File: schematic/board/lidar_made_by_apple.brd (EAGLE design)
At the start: 79.9 x 73.5 mm, 85 parts, among them J1 U.FL-R-SMT-1_10_, J2 U.FL-R-SMT-1_10_

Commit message: спонсор страданий
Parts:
- removed JP1, JP2: (no value), NEON-BLADE-2024:1X08
- removed W2: (no value), NEON-BLADE-2024:SOLDERING-PAD-4A
- added JP3: (no value), pinhead:1X15
- added JP4, JP5: (no value), pinhead:1X09
- added U$12, U$14: REF3033, NEON-BLADE-2024:SOT23-3
- added VR1, VR2: 3362P-1-502LF, NEON-BLADE-2024:TRIM_3362P-1-502LF
- added W5: (no value), NEON-BLADE-2024:SOLDERING-PAD-4A
- moved W1 38.3 mm to (22.7, 59.8)
- moved L9 18.0 mm to (38.1, 71.5)
- moved R30 13.8 mm to (37.9, 74.2), turned to 180 degrees
- moved C18 6.21 mm to (40.9, 77.2), turned to 180 degrees
- moved R21 5.83 mm to (48.3, 75.1)
- moved C9 5.10 mm to (68.2, 29.8)
- moved D2 4.58 mm to (65.8, 30.2), turned to 180 degrees
- moved C20 4.00 mm to (43.1, 73.0)
- moved C21 3.00 mm to (57.3, 69.4)
- moved C22 3.00 mm to (57.3, 72.7)
- moved C29 3.00 mm to (60.0, 69.9)
- moved R24 3.00 mm to (54.6, 70.6)
- moved R31 3.00 mm to (58.0, 66.7)
- moved U$10 3.00 mm to (48.0, 68.9)
- moved U$9 3.00 mm to (52.0, 70.5)
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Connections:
- removed net MISO: JP2.5, U$10.12
- removed net MOSI: JP2.6, U$10.11
- removed net SCK: JP2.4, U$10.10
- removed net SSN: JP2.3, U$10.9
- removed net VIN: L2.2, L4.1
- new net 1MISO: JP3.3
- new net 1MOSI: JP3.2
- new net 1SCK: JP3.1
- new net 4MISO: JP5.4, U$10.12
- new net 4MOSI: JP5.3, U$10.11
- new net 4SCK: JP5.2, U$10.10
- new net 5MISO: JP3.11
- new net 5MOSI: JP3.10
- new net 5SCK: JP3.9
- new net 5V: JP4.1
- new net CE_NRF: JP3.7
- new net CS_LIS: JP3.4
- new net CS_LSM: JP3.12
- new net CS_NRF: JP3.8
- new net CS_TDC: JP5.5, U$10.9
- new net N$28: JP3.13
- new net N$30: JP3.15
- new net N$33: R6.1, VR1.1
- new net N$35: R5.2, VR1.3
- new net N$37: R22.1, VR2.1
- new net N$38: R23.2, VR2.3
- new net SCL: JP4.9
- new net SDA: JP4.8
- new net SDIO_CK: JP4.5
- new net SDIO_CMD: JP4.4
- new net SDIO_DAT0: JP4.6
- new net SDIO_DAT1: JP4.7
- new net SDIO_DAT2: JP4.2
- new net SDIO_DAT3: JP4.3
- new net USIL_ON: JP5.1
- new net V_BAT: JP3.14, L2.2, L4.1, U$12.1, U$14.1
- net 3V3: now also JP3.5, U$12.2, U$14.2; no longer JP2.8
- net AGND: now also R26.1, U$12.3, U$14.3, W5.P$2
- net APD_FB_VOLT: now also JP5.8; no longer JP1.7
- net APD_PWM: now also JP5.9; no longer JP1.8
- net GND: now also JP3.6, W5.P$1; no longer JP2.7, R26.1, W2.P$2
- net LASER_COMP: now also JP5.6; no longer JP1.2
- net LGND: no longer W2.P$1
- net N$27: now also VR1.2; no longer R5.2, R6.1
- net N$5: now also VR2.2; no longer R22.1, R23.2
- net TDC_INT: now also JP5.7; no longer JP1.3

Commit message: переделал плату лидара
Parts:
- removed R4: 10k, rcl:R0603
- removed U$14: REF3033, NEON-BLADE-2024:SOT23-3
- moved C24 146.4 mm to (-69.8, 41.9), turned to 0 degrees
- moved C21 127.9 mm to (-68.6, 47.0), turned to 0 degrees
- moved C17 127.2 mm to (-62.2, 47.0)
- moved R1 99.4 mm to (-61.0, 62.2), turned to 0 degrees
- moved C22 77.9 mm to (-17.8, 52.1), turned to 0 degrees
- moved C33 72.4 mm to (-33.0, 35.6)
- moved R30 58.7 mm to (47.0, 16.2), turned to 90 degrees
- moved R21 57.1 mm to (43.5, 18.2), turned to 270 degrees
- moved L9 56.5 mm to (44.4, 15.3)
- moved C18 51.7 mm to (42.1, 25.5), turned to 0 degrees
- moved C20 51.4 mm to (42.1, 21.6)
- moved L2 49.2 mm to (65.2, 76.3), turned to 90 degrees
- moved C29 47.9 mm to (59.5, 22.0), turned to 0 degrees
- moved R31 46.8 mm to (59.5, 19.9), turned to 0 degrees
- moved R24 45.2 mm to (58.0, 25.5)
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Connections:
- removed net LASER_DAC: R4.2
- removed net LGND: C16.2, C17.1, C2.1, C9.1, J2.2, R16.1, R19.1, R6.2, U$1.P$4, U$1.P$5, U$11.GND, W1.P$1, W3.1
- removed net N$19: U$2.P$1, U$2.P$2
- new net 3V3_REF: C24.1, L10.1, L7.1, U$12.2, U$4.P$5
- new net PGND: C16.2, C17.1, C2.1, C6.2, C9.1, J2.2, R16.1, R19.1, R6.2, U$1.P$4, U$1.P$5, U$11.GND, W1.P$1, W3.1
- net 3V3: no longer C24.1, L10.1, L7.1, U$12.2, U$14.2, U$4.P$5
- net AGND: no longer U$14.3
- net GND: no longer C6.2
- net N$27: no longer R4.1
- net N$4: now also U$2.P$1, U$2.P$2
- net V_BAT: no longer U$14.1

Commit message: я сделял
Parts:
- moved C17 137.4 mm to (75.0, 54.5)
- moved C21 129.7 mm to (59.7, 28.0), turned to 180 degrees
- moved C24 118.3 mm to (48.4, 38.5), turned to 180 degrees
- moved R1 101.2 mm to (37.1, 37.0)
- moved C22 80.3 mm to (59.7, 31.0), turned to 180 degrees
- moved C33 67.0 mm to (34.0, 37.0), turned to 180 degrees
- moved R31 10.7 mm to (64.5, 29.3), turned to 90 degrees
- moved C29 7.87 mm to (62.4, 29.3), turned to 90 degrees
- moved U$2 7.12 mm to (75.7, 51.5), turned to 0 degrees
- moved R18 6.37 mm to (78.4, 54.5), turned to 0 degrees
- moved C19 6.21 mm to (57.5, 53.2), turned to 0 degrees
- moved R24 4.12 mm to (57.0, 29.5)
- moved U$9 4.12 mm to (54.5, 29.5)
- moved C16 2.83 mm to (78.2, 62.0), turned to 90 degrees
- moved C9 2.01 mm to (74.2, 71.0)
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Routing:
- net GND: track 0.00 -> 173.5 mm, vias 0 -> 8
- net 3V3: track 0.00 -> 130.0 mm, vias 0 -> 3
- net PGND: track 0.00 -> 85.2 mm, vias 0 -> 2
- net AGND: track 0.00 -> 66.7 mm, vias 0 -> 2
- net LASER_COMP: track 0.00 -> 62.5 mm, vias 0 -> 1
- net LASER_PULSE: track 0.00 -> 62.4 mm, vias 0 -> 3
- net V_BAT: track 0.00 -> 54.2 mm, vias 0 -> 2
- net APD_FB_VOLT: track 0.00 -> 53.8 mm, vias 0 -> 1
- net APD_PWM: track 0.00 -> 50.1 mm, vias 0 -> 1
- net TDC_INT: track 0.00 -> 46.3 mm
- net CS_TDC: track 0.00 -> 39.3 mm
- net I_LASER: track 0.00 -> 39.0 mm
- net APD_COMP_OUT: track 0.00 -> 37.4 mm
- net APD_V: track 0.00 -> 35.4 mm, vias 0 -> 2
- net VLASER: track 0.00 -> 34.5 mm
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
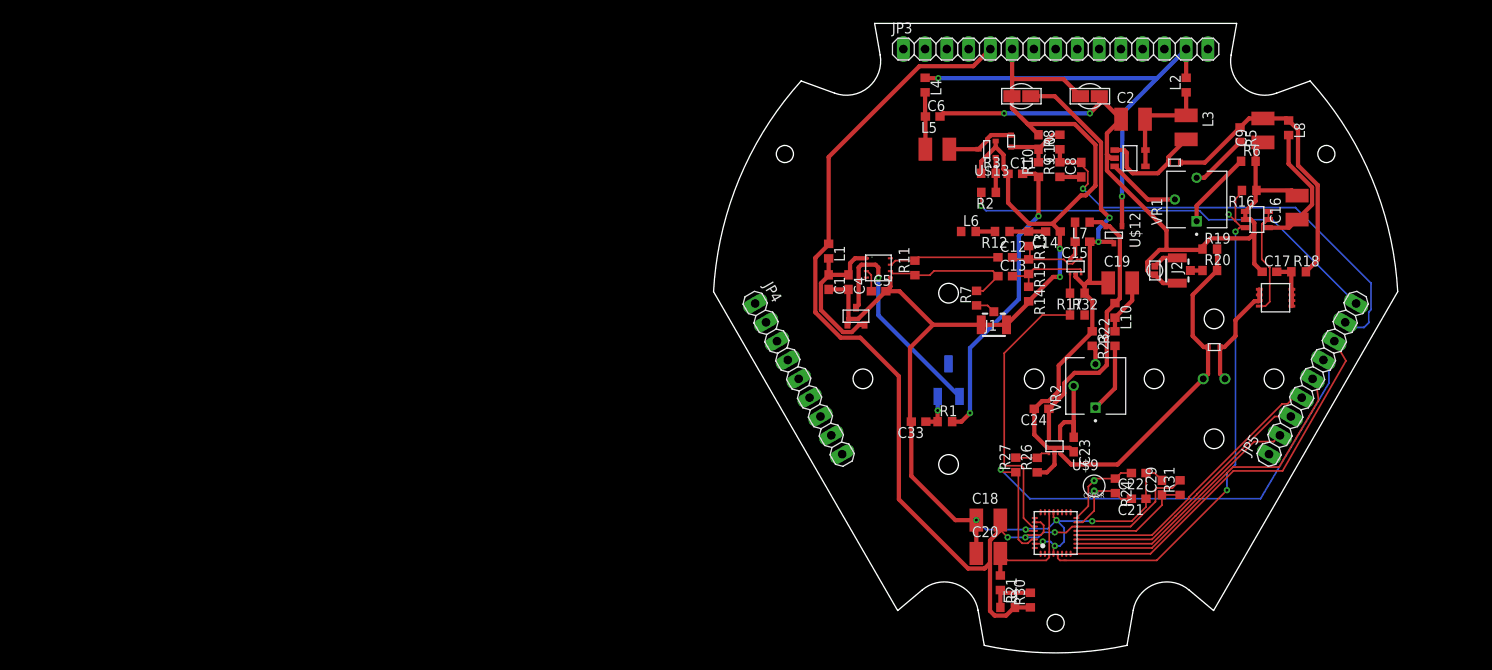
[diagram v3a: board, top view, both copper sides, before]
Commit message: немного переделал плату лидара
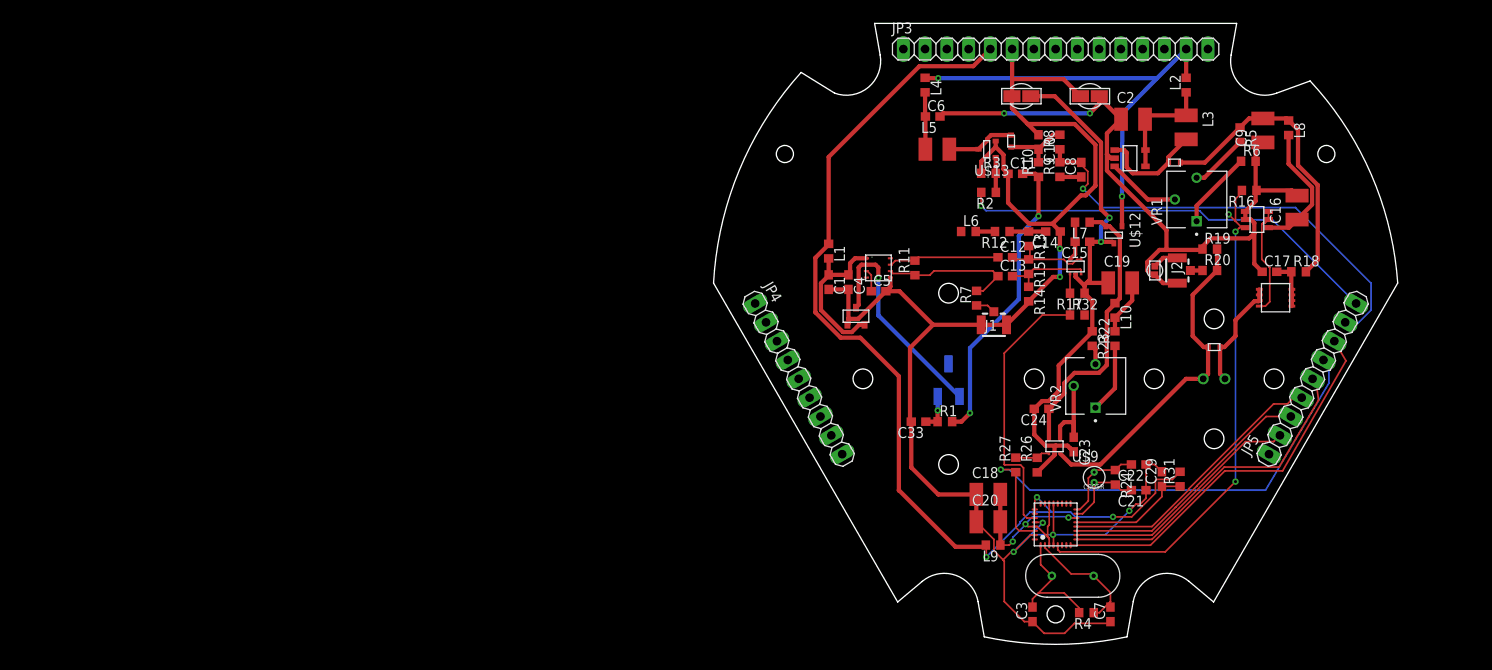
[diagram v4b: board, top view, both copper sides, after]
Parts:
- removed R21: 22, rcl:R0603
- removed R30: 0, rcl:R0603
- added C3, C7: 15pF, rcl:C0603
- added R4: 560k, rcl:R0603
- added U$14: HC49S, NEON-BLADE-2024:HC49S
- moved L9 7.48 mm to (42.7, 22.6), turned to 180 degrees
- moved C20 3.70 mm to (42.1, 25.3)
- moved C18 3.00 mm to (42.1, 28.5)
- moved C21 1.00 mm to (59.7, 29.0)
- moved C22 1.00 mm to (59.7, 32.0)
- moved C29 1.00 mm to (62.4, 30.3)
- moved R24 1.00 mm to (57.0, 30.5)
- moved R31 1.00 mm to (64.5, 30.3)
- moved U$10 1.00 mm to (50.0, 25.0)
- moved U$9 1.00 mm to (54.5, 30.5)
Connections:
- removed net N$24: L9.1, R21.2, R30.2
- removed net TDC_CLK: U$10.1
- new net N$19: C7.2, R4.1, U$10.2, U$14.P$1
- new net V_TDC: C18.2, C20.2, L9.1, U$10.14, U$10.22, U$10.29, U$10.3
- net 3V3: no longer C18.2, R30.1, U$10.14, U$10.29
- net GND: now also C3.1, C7.1
- net N$23: now also C3.2, R4.2, U$10.1, U$14.P$2; no longer C20.2, R21.1, U$10.22, U$10.3
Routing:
- net V_TDC: track 0.00 -> 25.5 mm, vias 0 -> 3
- net GND: track 173.5 -> 198.3 mm, vias 8 -> 6
- net N$19: track 0.00 -> 14.3 mm
- net 3V3: track 130.0 -> 116.1 mm
- net N$24: track 5.66 -> 0.00 mm
- net LASER_COMP: track 62.5 -> 60.1 mm
- net APD_FB_VOLT: track 53.8 -> 53.1 mm
- net N$23: track 14.0 -> 14.7 mm
- net APD_COMP_OUT: track 37.4 -> 36.7 mm
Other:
- board size 79.9 x 73.5 mm -> 79.9 x 72.5 mm

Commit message: ага угу
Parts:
- moved W5 31.9 mm to (63.0, 48.0), turned to 0 degrees
- moved U$5 5.00 mm to (32.3, 59.0)
- moved C1 5.00 mm to (26.5, 57.3)
- moved C4 5.00 mm to (28.8, 57.3)
- moved C5 5.00 mm to (32.3, 56.2)
- moved D6 5.00 mm to (29.7, 53.3)
- moved L1 5.00 mm to (26.5, 60.9)
- moved R11 5.00 mm to (36.6, 59.0)
- moved J2 2.00 mm to (66.2, 54.6)
- moved R19 2.00 mm to (70.0, 57.1)
- moved R20 2.00 mm to (70.0, 54.6)
- moved W3 2.00 mm to (63.6, 54.6)
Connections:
- net AGND: now also C1.2, C14.1, C33.2, C4.2, C5.2, D6.P$1, J1.1, J1.2, R14.2, U$5.P$5
- net GND: no longer C1.2, C10.1, C11.1, C14.1, C33.2, C4.2, C5.2, D6.P$1, J1.1, J1.2, R14.2, R3.1, U$13.2, U$5.P$5
- net PGND: now also C10.1, C11.1, R3.1, U$13.2
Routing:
- net GND: track 198.3 -> 129.4 mm, vias 6 -> 4
- net AGND: track 66.8 -> 128.5 mm
- net APD_V: track 35.4 -> 83.9 mm
- net PGND: track 85.2 -> 116.2 mm
- net APD_FB_VOLT: track 53.1 -> 57.4 mm
- net 3V3: track 116.1 -> 112.3 mm
- net N$8: track 26.4 -> 29.1 mm
- net I_LASER: track 39.0 -> 40.8 mm, vias 0 -> 1
- net N$11: track 16.4 -> 14.7 mm
- net APD_PWM: track 50.1 -> 51.0 mm
- net LASER_PULSE: track 61.9 -> 62.8 mm

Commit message: Безумие — это точное повторение одного и того же действия раз за разом в надежде на изменение
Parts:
- moved L9 55.4 mm to (43.1, 78.0)
- moved U$10 48.3 mm to (49.0, 73.3)
- moved U$14 47.8 mm to (47.5, 66.6)
- moved R4 47.8 mm to (47.5, 62.1)
- moved C18 46.5 mm to (42.5, 75.0)
- moved C20 46.5 mm to (42.5, 71.8)
- moved L4 46.3 mm to (58.0, 36.2)
- moved C7 45.2 mm to (48.6, 59.0)
- moved C6 44.9 mm to (60.6, 35.3)
- moved C3 44.5 mm to (46.4, 59.0)
- moved C21 44.3 mm to (59.1, 73.3)
- moved C22 44.3 mm to (59.1, 76.3)
- moved R24 44.3 mm to (56.4, 74.8)
- moved U$9 44.3 mm to (53.9, 74.8)
- moved D1 44.0 mm to (60.8, 28.8)
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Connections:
- net 3V3: no longer L1.1, R31.2, U$10.25, U$10.26
- net 3V3_REF: now also L1.1
- net V_TDC: now also R31.2, U$10.25, U$10.26
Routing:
- net 3V3: track 112.3 -> 2.56 mm, vias 3 -> 0
- net APD_V: track 83.9 -> 23.2 mm, vias 2 -> 0
- net GND: track 129.4 -> 69.9 mm, vias 4 -> 3
- net PGND: track 116.2 -> 165.6 mm, vias 2 -> 0
- net 3V3_REF: track 33.0 -> 70.1 mm, vias 0 -> 2
- net VLASER: track 34.5 -> 8.81 mm
- net APD_FB_VOLT: track 57.4 -> 33.1 mm, vias 1 -> 0
- net I_LASER: track 40.8 -> 17.8 mm, vias 1 -> 0
- net LASER_PULSE: track 62.8 -> 40.0 mm, vias 3 -> 2
- net N$17: track 4.22 -> 24.7 mm
- net 4SCK: track 28.6 -> 48.9 mm, vias 0 -> 1
- net 4MISO: track 32.6 -> 52.1 mm, vias 0 -> 1
- net 4MOSI: track 30.6 -> 50.0 mm, vias 0 -> 1
- net N$8: track 29.1 -> 11.7 mm
- net N$13: track 4.32 -> 19.8 mm
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- added copper zone on layer 16, net AGND
- added copper zone on layer 16, net GND
- added copper zone on layer 16, net PGND
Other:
- outline, holes or cut-outs redrawn

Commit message: Даниил на протяжении 510 лет переделывает плату лидара
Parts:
- moved C3 2.70 mm to (44.9, 61.2)
- moved C7 2.70 mm to (50.1, 61.2)
- moved C16 1.00 mm to (78.4, 62.1)
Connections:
- net 5V: now also U$12.1
- net V_BAT: no longer U$12.1
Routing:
- net 5V: track 0.00 -> 43.6 mm, vias 0 -> 1
- net V_BAT: track 65.0 -> 73.6 mm, vias 3 -> 2
- net LASER_COMP: track 73.8 -> 72.0 mm, vias 3 -> 4
- net APD_COMP_OUT: track 37.6 -> 39.2 mm
- net PGND: track 165.6 -> 164.2 mm
- net N$23: track 12.7 -> 12.1 mm
- net N$19: track 12.7 -> 12.1 mm

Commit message: почти добавил новый разъём
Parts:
- removed JP3: (no value), pinhead:1X15
- removed JP4, JP5: (no value), pinhead:1X09
- added U$15, U$16: PBS_SMD_X9, NEON-BLADE-2024:PBS_SMD_X9
- added U$17: PBS_SMD_X15, NEON-BLADE-2024:PBD_SMD_X15
- moved C21 3.24 mm to (62.3, 73.8)
- moved C22 3.22 mm to (62.3, 75.9)
- moved L9 1.17 mm to (42.5, 77.0)
- moved C18 1.00 mm to (42.5, 74.0)
- moved C20 1.00 mm to (42.5, 70.8)
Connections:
- net 1MISO: now also U$17.3; no longer JP3.3
- net 1MOSI: now also U$17.2; no longer JP3.2
- net 1SCK: now also U$17.1; no longer JP3.1
- net 3V3: now also U$17.5; no longer JP3.5
- net 4MISO: now also U$15.4; no longer JP5.4
- net 4MOSI: now also U$15.3; no longer JP5.3
- net 4SCK: now also U$15.2; no longer JP5.2
- net 5MISO: now also U$17.11; no longer JP3.11
- net 5MOSI: now also U$17.10; no longer JP3.10
- net 5SCK: now also U$17.9; no longer JP3.9
- net 5V: now also U$16.1; no longer JP4.1
- net APD_FB_VOLT: now also U$15.8; no longer JP5.8
- net APD_PWM: now also U$15.9; no longer JP5.9
- net CE_NRF: now also U$17.7; no longer JP3.7
- net CS_LIS: now also U$17.4; no longer JP3.4
- net CS_LSM: now also U$17.12; no longer JP3.12
- net CS_NRF: now also U$17.8; no longer JP3.8
- net CS_TDC: now also U$15.5; no longer JP5.5
- net GND: now also U$17.6; no longer JP3.6
- net LASER_COMP: now also U$15.6; no longer JP5.6
- net N$28: now also U$17.13; no longer JP3.13
- net N$30: now also U$17.15; no longer JP3.15
- net SCL: now also U$16.9; no longer JP4.9
- net SDA: now also U$16.8; no longer JP4.8
- net SDIO_CK: now also U$16.5; no longer JP4.5
- net SDIO_CMD: now also U$16.4; no longer JP4.4
- net SDIO_DAT0: now also U$16.6; no longer JP4.6
- net SDIO_DAT1: now also U$16.7; no longer JP4.7
- net SDIO_DAT2: now also U$16.2; no longer JP4.2
- net SDIO_DAT3: now also U$16.3; no longer JP4.3
- net TDC_INT: now also U$15.7; no longer JP5.7
- net USIL_ON: now also U$15.1; no longer JP5.1
- net V_BAT: now also U$17.14; no longer JP3.14
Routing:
- net GND: track 70.0 -> 77.0 mm
- net N$25: track 7.36 -> 10.4 mm
- net N$22: track 7.33 -> 10.3 mm
- net 5V: track 43.6 -> 41.5 mm, vias 1 -> 2
- net 4MOSI: track 50.0 -> 48.1 mm, vias 1 -> 2
- net APD_PWM: track 47.1 -> 45.4 mm, vias 1 -> 2
- net TDC_INT: track 44.9 -> 43.2 mm, vias 1 -> 2
- net V_TDC: track 28.7 -> 30.3 mm
- net LASER_COMP: track 72.0 -> 73.3 mm, vias 4 -> 5
- net 3V3: track 2.56 -> 3.85 mm
- net APD_FB_VOLT: track 33.1 -> 31.9 mm
- net 4SCK: track 48.9 -> 50.1 mm, vias 1 -> 2
- net CS_TDC: track 45.8 -> 44.9 mm, vias 1 -> 2
- net 4MISO: track 52.1 -> 52.2 mm, vias 1 -> 2
